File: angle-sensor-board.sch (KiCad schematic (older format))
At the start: 8 parts, among them J1 Picoblade 5 pin, U1 AS5055A

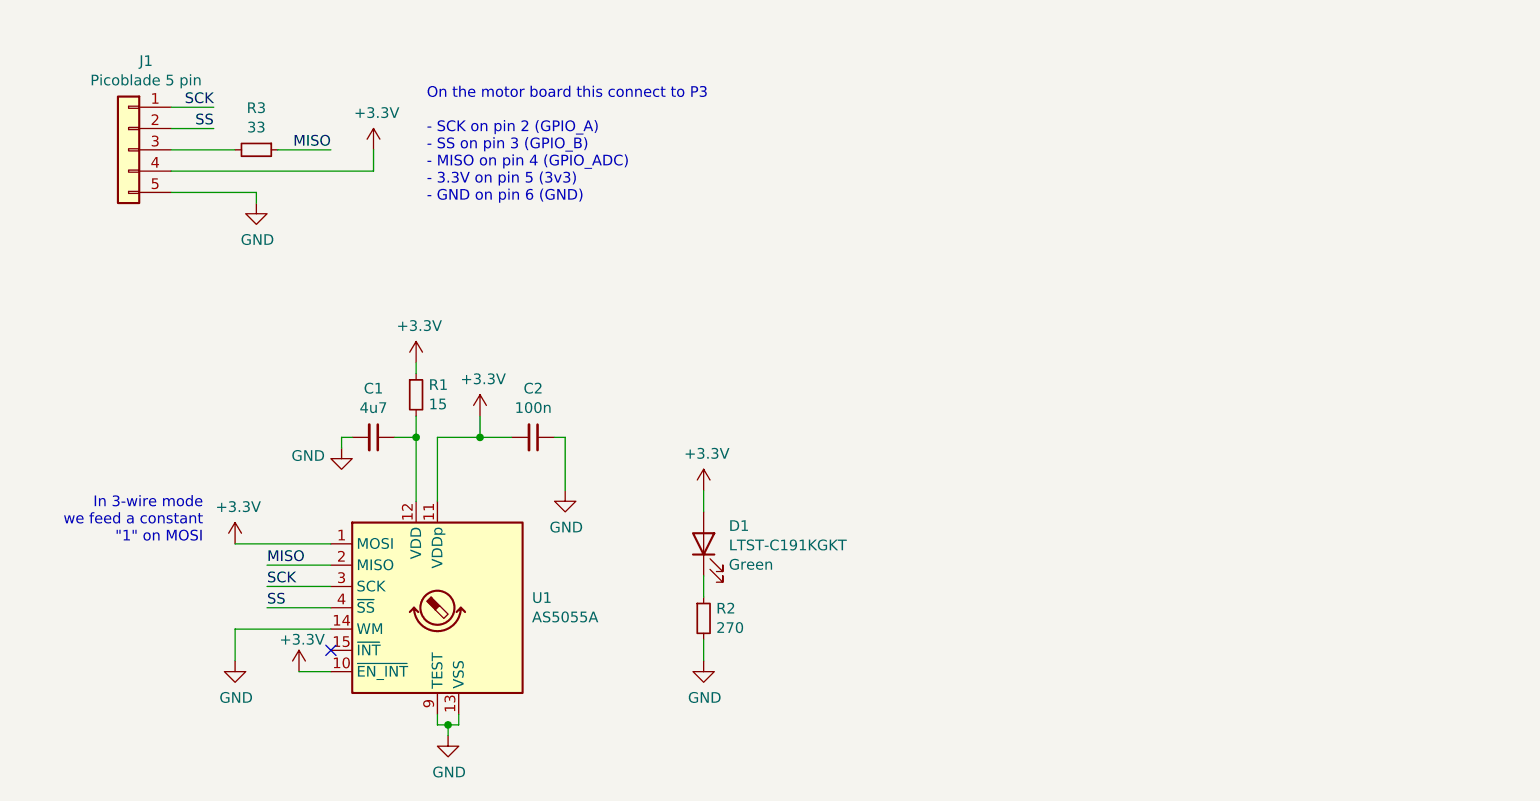
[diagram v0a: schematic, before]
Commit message: Add digikey references for passives
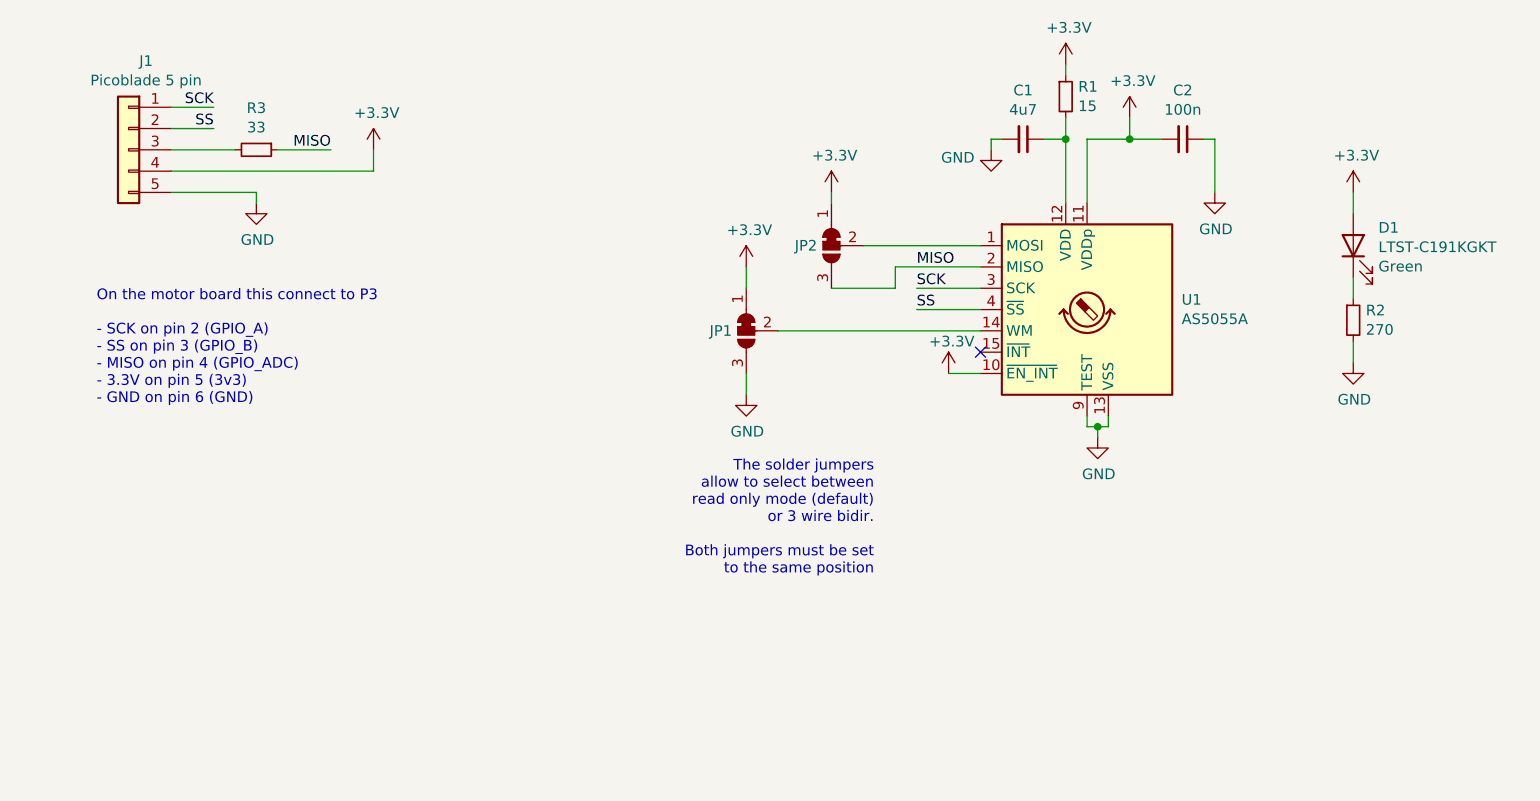
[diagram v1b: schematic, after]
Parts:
- added JP1, JP2: SolderJumper_3_Bridged12, Jumper:SolderJumper-3_P1.3mm_Bridged12_RoundedPad1.0x1.5mm, symbol Jumper:SolderJumper_3_Bridged12
- C1: digikey# (none) -> 1276-1045-1-ND
- C2: digikey# (none) -> 1276-1006-1-ND
- R1: digikey# (none) -> A129666CT-ND
- R2: digikey# (none) -> A129681CT-ND
- R3: digikey# (none) -> A130082CT-ND
- U1: digikey# (none) -> AS5055A-BQFMCT-ND
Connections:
- net +3V3: now also JP1.1 (A), JP2.1 (A); no longer U1.1 (MOSI)
- net GND: now also JP1.3 (B); no longer U1.14 (WM)
- net MISO: now also JP2.3 (B)
- new net: JP2.2 (C), U1.1 (MOSI)
- new net: JP1.2 (C), U1.14 (WM)
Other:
- note added: "The solder jumpers\nallow to select between\nread only mode (default)\nor 3 wire bidir.\n\nBoth jumpers must be set\nto the same position"
- note removed: "In 3-wire mode\nwe feed a constant\n"1" on MOSI"
- moved on the sheet: C1, C2, D1, R1, R2, U1
